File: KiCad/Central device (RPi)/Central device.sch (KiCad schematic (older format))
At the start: 1 part

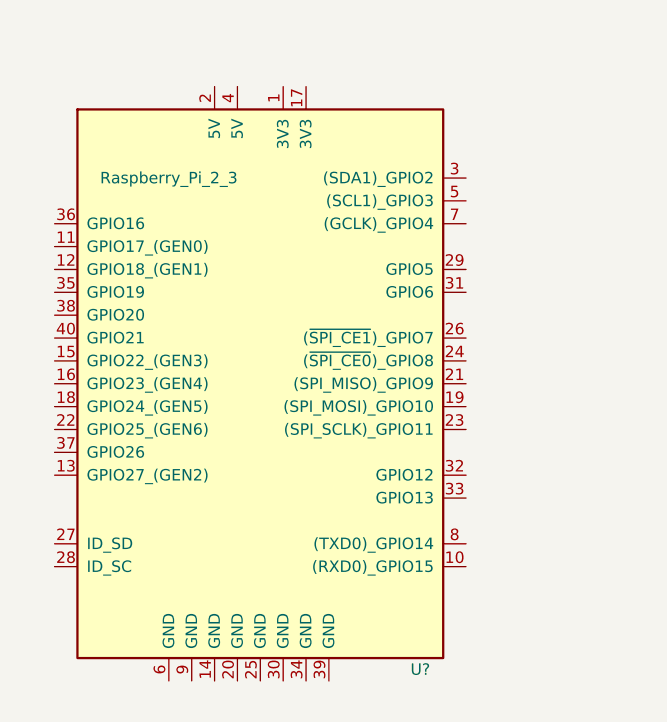
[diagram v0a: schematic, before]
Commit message: Added DHT11
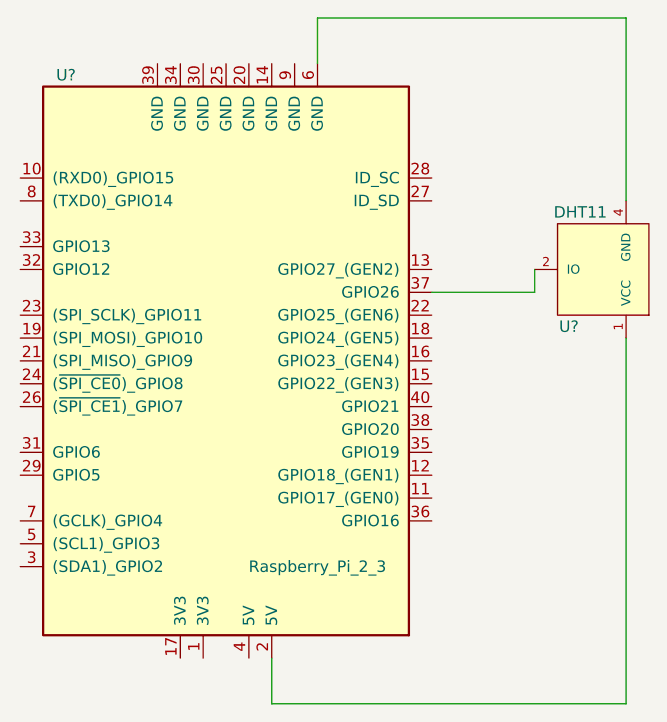
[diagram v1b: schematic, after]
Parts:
- added U?: DHT11, symbol DHT11
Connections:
- net at U?.2 (5V): now also U?.1 (VCC)
- net at U?.37 (GPIO26): now also U?.2 (IO)
- net at U?.6 (GND): now also U?.4 (GND)
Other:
- moved on the sheet: U?
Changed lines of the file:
@@
 LIBS:contrib
 LIBS:valves
+LIBS:sensors
+LIBS:Central device-cache
 EELAYER 25 0
 EELAYER END
@@
 L Raspberry_Pi_2_3 U?
 U 1 1 59353BE3
-P 3700 3100
-F 0 "U?" H 4400 1850 50  0000 C CNN
-F 1 "Raspberry_Pi_2_3" H 3300 4000 50  0000 C CNN
-F 2 "Pin_Headers:Pin_Header_Straight_2x20" H 4700 4350 50  0001 C CNN
-F 3 "" H 3750 2950 50  0001 C CNN
-	1    3700 3100
-	1    0    0    -1
+P 3550 3000
+F 0 "U?" H 4250 1750 50  0000 C CNN
+F 1 "Raspberry_Pi_2_3" H 3150 3900 50  0000 C CNN
+F 2 "Pin_Headers:Pin_Header_Straight_2x20" H 4550 4250 50  0001 C CNN
+F 3 "" H 3600 2850 50  0001 C CNN
+	1    3550 3000
+	-1   0    0    1
 $EndComp
+$Comp
+L DHT11 U?
+U 1 1 593E3675
+P 5200 2600
+F 0 "U?" H 5350 2850 50  0000 C CNN
+F 1 "DHT11" H 5300 2350 50  0000 C CNN
+F 2 "" H 5350 2850 50  0001 C CNN
+F 3 "" H 5350 2850 50  0001 C CNN
+	1    5200 2600
+	-1   0    0    1
+$EndComp
+Wire Wire Line
+	3750 4300 3750 4500
+Wire Wire Line
+	3750 4500 5300 4500
+Wire Wire Line
+	5300 4500 5300 2900
+Wire Wire Line
+	5300 2300 5300 1500
+Wire Wire Line
+	5300 1500 3950 1500
+Wire Wire Line
+	3950 1500 3950 1700
+Wire Wire Line
+	4900 2600 4900 2700
+Wire Wire Line
+	4900 2700 4450 2700
 $EndSCHEMATC

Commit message: Almost finished kicad schema of central device
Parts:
- added DS?: LCD-016N002L, WC1602A, symbol LCD-016N002L
- added U?: PCF8574A, symbol PCF8574A
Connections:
- net at U?.3 ((SDA1)_GPIO2): now also U?.15 (SDA)
- net at U?.37 (GPIO26): no longer U?.2 (IO)
- net at U?.4 (5V): now also DS?.15 (LED+), DS?.2 (VDD), U?.16 (VDD)
- net at U?.5 ((SCL1)_GPIO3): now also U?.14 (SCL)
- net at U?.7 ((GCLK)_GPIO4): now also U?.2 (IO)
- net at U?.9 (GND): now also DS?.1 (VSS), DS?.16 (LED-), U?.8 (VSS)
- new net: DS?.12 (D5), U?.10 (P5)
- new net: DS?.13 (D6), U?.11 (P6)
- new net: DS?.14 (D7), U?.12 (P7)
- new net: DS?.7 (D0), U?.4 (P0)
- new net: DS?.8 (D1), U?.5 (P1)
- new net: DS?.9 (D2), U?.6 (P2)
- new net: DS?.10 (D3), U?.7 (P3)
- new net: DS?.11 (D4), U?.9 (P4)
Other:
- note added: "These two components are already unified in one single product.\nConnection between them come from my imagination.\n(Need help to get the good connection)."
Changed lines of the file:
@@
 	3950 1500 3950 1700
 Wire Wire Line
-	4900 2600 4900 2700
+	4900 2600 4800 2600
 Wire Wire Line
-	4900 2700 4450 2700
+	4800 2600 4800 4450
+Wire Wire Line
+	4800 4450 2500 4450
+Wire Wire Line
+	2500 4450 2500 3700
+Wire Wire Line
+	2500 3700 2650 3700
+$Comp
+L PCF8574A U?
+U 1 1 5946C7CE
+P 6600 3800
+F 0 "U?" H 6250 4400 50  0000 L CNN
+F 1 "PCF8574A" H 6700 4400 50  0000 L CNN
+F 2 "" H 6600 3800 50  0000 C CNN
+F 3 "" H 6600 3800 50  0000 C CNN
+	1    6600 3800
+	1    0    0    -1
+$EndComp
+Wire Wire Line
+	6100 3400 4850 3400
+Wire Wire Line
+	4850 3400 4850 4400
+Wire Wire Line
+	4850 4400 2550 4400
+Wire Wire Line
+	2550 4400 2550 3800
+Wire Wire Line
+	2550 3800 2650 3800
+Wire Wire Line
+	6100 3500 4900 3500
+Wire Wire Line
+	4900 3500 4900 4350
+Wire Wire Line
+	4900 4350 2600 4350
+Wire Wire Line
+	2600 4350 2600 3900
+Wire Wire Line
+	2600 3900 2650 3900
+Wire Wire Line
+	3650 4300 3650 4550
+Wire Wire Line
+	6600 4550 6600 4500
+Wire Wire Line
+	6600 3100 6600 3050
+Wire Wire Line
+	5950 3050 9250 3050
+Wire Wire Line
+	5950 3050 5950 4550
+$Comp
+L LCD-016N002L DS?
+U 1 1 5946CA00
+P 8600 2350
+F 0 "DS?" H 7800 2750 50  0000 C CNN
+F 1 "LCD-016N002L" H 9300 2750 50  0000 C CNN
+F 2 "WC1602A" H 8600 2300 50  0000 C CIN
+F 3 "" H 8600 2350 50  0000 C CNN
+	1    8600 2350
+	1    0    0    -1
+$EndComp
+Wire Wire Line
+	7950 3050 7950 2850
+Connection ~ 6600 3050
+Wire Wire Line
+	7850 4550 7850 2850
+Wire Wire Line
+	7100 3400 8450 3400
+Wire Wire Line
+	8450 3400 8450 2850
+Wire Wire Line
+	7100 3500 8550 3500
+Wire Wire Line
+	8550 3500 8550 2850
+Wire Wire Line
+	7100 3600 8650 3600
+Wire Wire Line
+	8650 3600 8650 2850
+Wire Wire Line
+	7100 3700 8750 3700
+Wire Wire Line
+	8750 3700 8750 2850
+Wire Wire Line
+	7100 3800 8850 3800
+Wire Wire Line
+	8850 3800 8850 2850
+Wire Wire Line
+	7100 3900 8950 3900
+Wire Wire Line
+	8950 3900 8950 2850
+Wire Wire Line
+	7100 4000 9050 4000
+Wire Wire Line
+	9050 4000 9050 2850
+Wire Wire Line
+	7100 4100 9150 4100
+Wire Wire Line
+	9150 4100 9150 2850
+Wire Wire Line
+	5950 4550 3650 4550
+Wire Wire Line
+	6200 4550 9350 4550
+Wire Wire Line
+	3850 1700 3850 1450
+Wire Wire Line
+	3850 1450 5500 1450
+Wire Wire Line
+	5500 1450 5500 4500
+Wire Wire Line
+	6200 4500 6200 4550
+Connection ~ 6600 4550
+Wire Wire Line
+	5500 4500 6200 4500
+Wire Wire Line
+	9250 3050 9250 2850
+Connection ~ 7950 3050
+Wire Wire Line
+	9350 4550 9350 2850
+Connection ~ 7850 4550
+Wire Notes Line
+	6050 1800 6050 4800
+Wire Notes Line
+	6050 4800 9750 4800
+Wire Notes Line
+	9750 4800 9750 1800
+Wire Notes Line
+	9750 1800 6050 1800
+Text Notes 6100 1750 0    60   ~ 0
+These two components are already unified in one single product.\nConnection between them come from my imagination.\n(Need help to get the good connection).
 $EndSCHEMATC

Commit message: Added relay
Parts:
- added K?: FINDER-32.21-x000, Relays_THT:Relay_SPST_Finder_32.21-x300, symbol FINDER-32.21-x000
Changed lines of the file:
@@
 LIBS:valves
 LIBS:sensors
+LIBS:switches
+LIBS:relays
 LIBS:Central device-cache
 EELAYER 25 0
@@
 Text Notes 6100 1750 0    60   ~ 0
 These two components are already unified in one single product.\nConnection between them come from my imagination.\n(Need help to get the good connection).
+$Comp
+L FINDER-32.21-x000 K?
+U 1 1 594776D9
+P 3450 5750
+F 0 "K?" H 3900 5900 50  0000 L CNN
+F 1 "FINDER-32.21-x000" H 3900 5800 50  0000 L CNN
+F 2 "Relays_THT:Relay_SPST_Finder_32.21-x300" H 4720 5720 50  0001 C CNN
+F 3 "" H 3450 5750 50  0001 C CNN
+	1    3450 5750
+	1    0    0    -1
+$EndComp
 $EndSCHEMATC

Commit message: Finished circuit draft (Central device)
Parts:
- added NPN1: Q_NPN_BCE, symbol Q_NPN_BCE
- gave numbers to parts that had none: 4
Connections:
- net at RPI1B+.29 (GPIO5): now also NPN1.1 (B)
- net at RPI1B+.39 (GND): now also NPN1.2 (C)
- net at LCD.15 (LED+), LCD.2 (VDD), LCDDriver.16 (VDD)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: now also RL1.A1
- net ToHeater: now reaches RL1.11
- net ToHeater: now also RL1.14
- net at RL1.A2: now also NPN1.3 (E)
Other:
- note added: "Unified component. Reverse engineered."
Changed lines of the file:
@@
 $EndDescr
 $Comp
-L Raspberry_Pi_2_3 U?
+L Raspberry_Pi_2_3 RPI1B+
 U 1 1 59353BE3
 P 3550 3000
-F 0 "U?" H 4250 1750 50  0000 C CNN
+F 0 "RPI1B+" H 4250 1750 50  0000 C CNN
 F 1 "Raspberry_Pi_2_3" H 3150 3900 50  0000 C CNN
 F 2 "Pin_Headers:Pin_Header_Straight_2x20" H 4550 4250 50  0001 C CNN
@@
 	2500 3700 2650 3700
 $Comp
-L PCF8574A U?
+L PCF8574A LCDDriver
 U 1 1 5946C7CE
 P 6600 3800
-F 0 "U?" H 6250 4400 50  0000 L CNN
+F 0 "LCDDriver" H 6250 4400 50  0000 L CNN
 F 1 "PCF8574A" H 6700 4400 50  0000 L CNN
 F 2 "" H 6600 3800 50  0000 C CNN
@@
 	2600 3900 2650 3900
 Wire Wire Line
-	3650 4300 3650 4550
+	3650 4300 3650 4850
 Wire Wire Line
 	6600 4550 6600 4500
@@
 	5950 3050 5950 4550
 $Comp
-L LCD-016N002L DS?
+L LCD-016N002L LCD
 U 1 1 5946CA00
 P 8600 2350
-F 0 "DS?" H 7800 2750 50  0000 C CNN
+F 0 "LCD" H 7800 2750 50  0000 C CNN
 F 1 "LCD-016N002L" H 9300 2750 50  0000 C CNN
 F 2 "WC1602A" H 8600 2300 50  0000 C CIN
@@
 These two components are already unified in one single product.\nConnection between them come from my imagination.\n(Need help to get the good connection).
 $Comp
-L FINDER-32.21-x000 K?
+L FINDER-32.21-x000 RL1
 U 1 1 594776D9
 P 3450 5750
-F 0 "K?" H 3900 5900 50  0000 L CNN
+F 0 "RL1" H 3900 5900 50  0000 L CNN
 F 1 "FINDER-32.21-x000" H 3900 5800 50  0000 L CNN
 F 2 "Relays_THT:Relay_SPST_Finder_32.21-x300" H 4720 5720 50  0001 C CNN
@@
 	1    0    0    -1
 $EndComp
+$Comp
+L Q_NPN_BCE NPN1
+U 1 1 594A1450
+P 2350 5750
+F 0 "NPN1" H 2550 5800 50  0000 L CNN
+F 1 "Q_NPN_BCE" H 2550 5700 50  0000 L CNN
+F 2 "" H 2550 5850 50  0000 C CNN
+F 3 "" H 2350 5750 50  0000 C CNN
+	1    2350 5750
+	1    0    0    -1
+$EndComp
+Wire Wire Line
+	2450 5950 2450 6400
+Wire Wire Line
+	2450 6400 3250 6400
+Wire Wire Line
+	3250 6400 3250 6050
+Wire Wire Line
+	3250 5450 3250 4850
+Wire Wire Line
+	3250 4850 3650 4850
+Connection ~ 3650 4550
+Wire Wire Line
+	2450 5550 2450 1450
+Wire Wire Line
+	2450 1450 3250 1450
+Wire Wire Line
+	3250 1450 3250 1700
+Wire Wire Line
+	2150 5750 2150 3500
+Wire Wire Line
+	2150 3500 2650 3500
+Wire Wire Line
+	3750 5450 3750 5250
+Wire Wire Line
+	3750 5250 5300 5250
+Wire Wire Line
+	5300 5250 5300 5800
+Wire Wire Line
+	3650 6050 3650 6300
+Wire Wire Line
+	3650 6300 5300 6300
+Wire Wire Line
+	5300 6300 5300 6150
+Text GLabel 5300 5800 2    60   Input ~ 0
+ToHeater
+Text GLabel 5300 6150 2    60   Input ~ 0
+ToHeater
+Wire Notes Line
+	1900 5100 5900 5100
+Wire Notes Line
+	5900 5100 5900 6700
+Wire Notes Line
+	5900 6700 1900 6700
+Wire Notes Line
+	1900 6700 1900 5100
+Text Notes 3750 6850 2    60   ~ 0
+Unified component. Reverse engineered.
 $EndSCHEMATC

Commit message: Finished circuit draft (Central device)
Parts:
- gave numbers to parts that had none: 1
- renumbered LCD to LCD1, LCDDriver to LCDDriver1, RPI1B+ to RPI1B+1
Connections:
- no-connect marks 0 -> 40
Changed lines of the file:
@@
 $EndDescr
 $Comp
-L Raspberry_Pi_2_3 RPI1B+
+L Raspberry_Pi_2_3 RPI1B+1
 U 1 1 59353BE3
 P 3550 3000
-F 0 "RPI1B+" H 4250 1750 50  0000 C CNN
+F 0 "RPI1B+1" H 4250 1750 50  0000 C CNN
 F 1 "Raspberry_Pi_2_3" H 3150 3900 50  0000 C CNN
 F 2 "Pin_Headers:Pin_Header_Straight_2x20" H 4550 4250 50  0001 C CNN
@@
 $EndComp
 $Comp
-L DHT11 U?
+L DHT11 U1
 U 1 1 593E3675
 P 5200 2600
-F 0 "U?" H 5350 2850 50  0000 C CNN
+F 0 "U1" H 5350 2850 50  0000 C CNN
 F 1 "DHT11" H 5300 2350 50  0000 C CNN
 F 2 "" H 5350 2850 50  0001 C CNN
@@
 	2500 3700 2650 3700
 $Comp
-L PCF8574A LCDDriver
+L PCF8574A LCDDriver1
 U 1 1 5946C7CE
 P 6600 3800
-F 0 "LCDDriver" H 6250 4400 50  0000 L CNN
+F 0 "LCDDriver1" H 6250 4400 50  0000 L CNN
 F 1 "PCF8574A" H 6700 4400 50  0000 L CNN
 F 2 "" H 6600 3800 50  0000 C CNN
@@
 	5950 3050 5950 4550
 $Comp
-L LCD-016N002L LCD
+L LCD-016N002L LCD1
 U 1 1 5946CA00
 P 8600 2350
-F 0 "LCD" H 7800 2750 50  0000 C CNN
+F 0 "LCD1" H 7800 2750 50  0000 C CNN
 F 1 "LCD-016N002L" H 9300 2750 50  0000 C CNN
 F 2 "WC1602A" H 8600 2300 50  0000 C CIN
@@
 Text Notes 3750 6850 2    60   ~ 0
 Unified component. Reverse engineered.
+NoConn ~ 3550 5450
+NoConn ~ 3350 1700
+NoConn ~ 3450 1700
+NoConn ~ 3550 1700
+NoConn ~ 3650 1700
+NoConn ~ 3750 1700
+NoConn ~ 2650 2200
+NoConn ~ 2650 2300
+NoConn ~ 2650 2500
+NoConn ~ 2650 2600
+NoConn ~ 2650 2800
+NoConn ~ 2650 2900
+NoConn ~ 2650 3000
+NoConn ~ 2650 3100
+NoConn ~ 2650 3200
+NoConn ~ 2650 3400
+NoConn ~ 3350 4300
+NoConn ~ 3450 4300
+NoConn ~ 4450 3700
+NoConn ~ 4450 3600
+NoConn ~ 4450 3500
+NoConn ~ 4450 3400
+NoConn ~ 4450 3300
+NoConn ~ 4450 3200
+NoConn ~ 4450 3100
+NoConn ~ 4450 3000
+NoConn ~ 4450 2900
+NoConn ~ 4450 2800
+NoConn ~ 4450 2700
+NoConn ~ 4450 2600
+NoConn ~ 4450 2300
+NoConn ~ 4450 2200
+NoConn ~ 6100 3700
+NoConn ~ 6100 3800
+NoConn ~ 6100 3900
+NoConn ~ 6100 4200
+NoConn ~ 8050 2850
+NoConn ~ 8150 2850
+NoConn ~ 8250 2850
+NoConn ~ 8350 2850
 $EndSCHEMATC

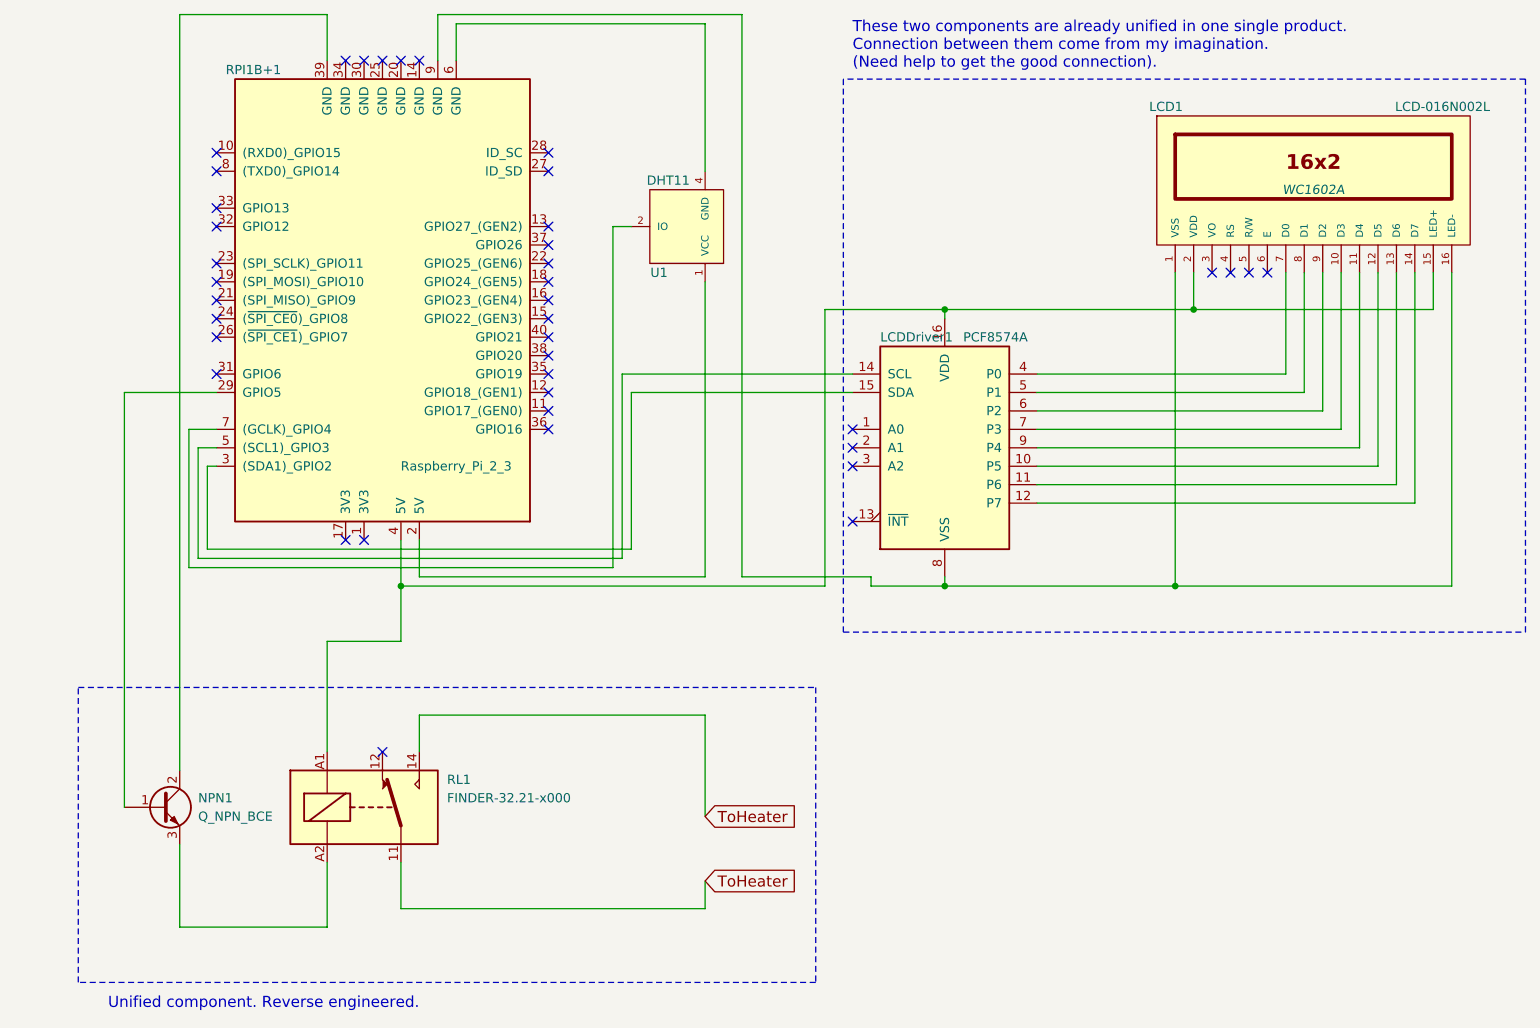
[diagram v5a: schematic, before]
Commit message: Added PDF of schema with corrections
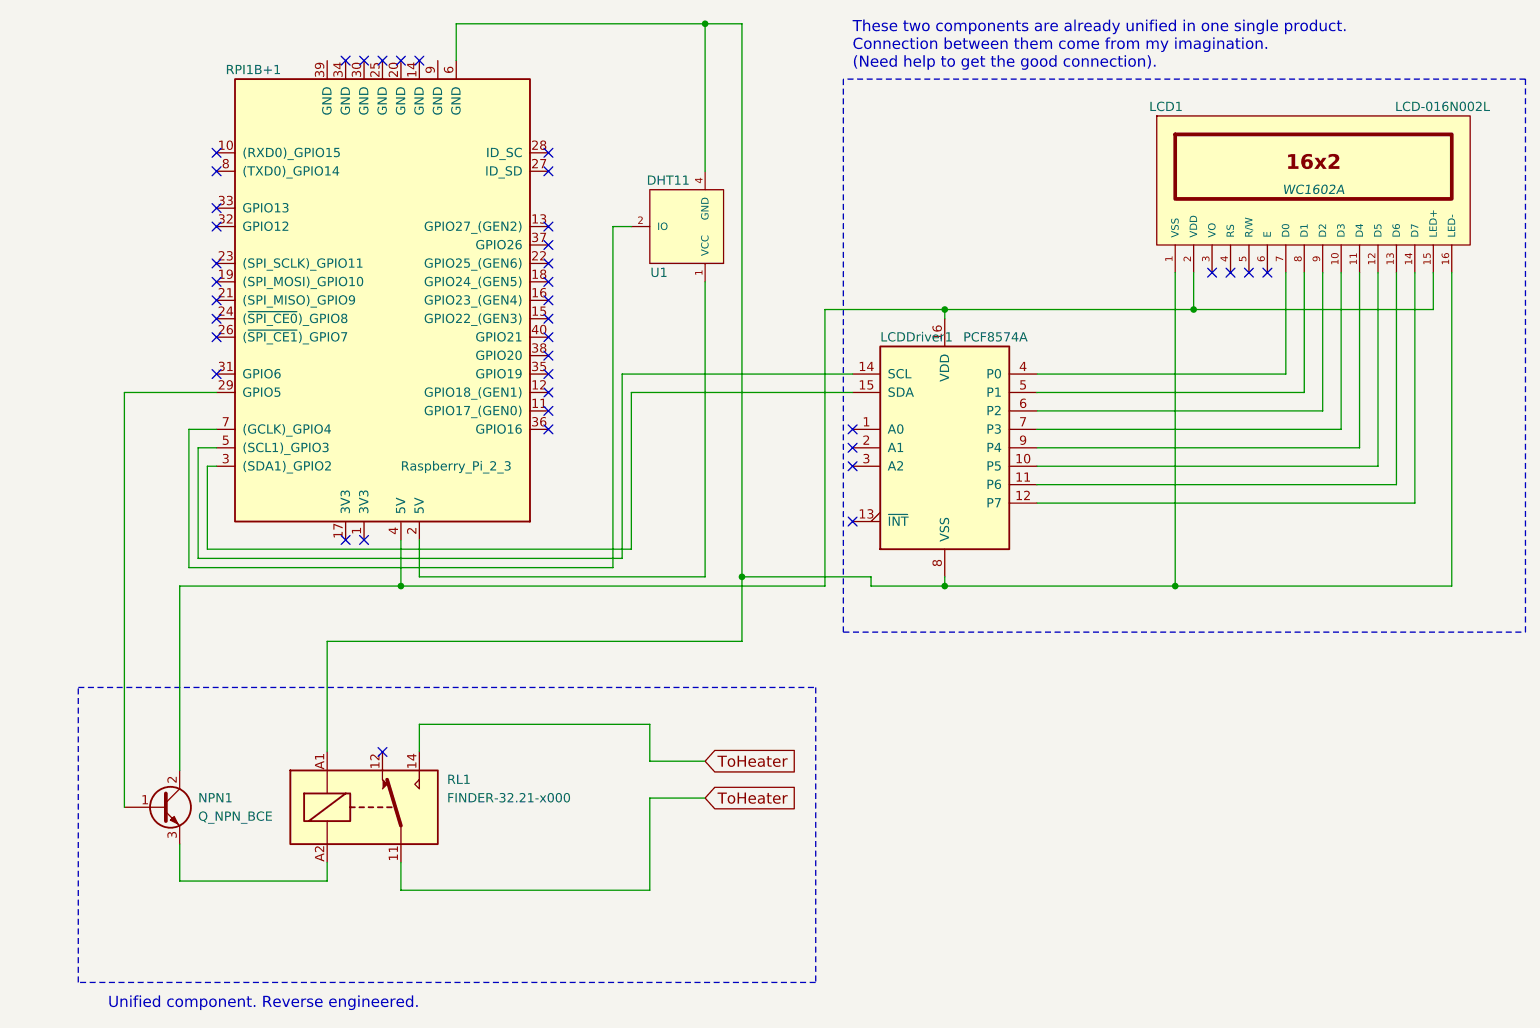
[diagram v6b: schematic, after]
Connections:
- net at RPI1B+1.39 (GND): no longer NPN1.2 (C)
- net at LCD1.15 (LED+), LCD1.2 (VDD), LCDDriver1.16 (VDD)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: now also NPN1.2 (C); no longer RL1.A1
- net at RPI1B+1.6 (GND), U1.4 (GND): now also LCD1.1 (VSS), LCD1.16 (LED-), LCDDriver1.8 (VSS), RL1.A1
- now unconnected: RPI1B+1.9 (GND)
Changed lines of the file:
@@
 	5300 2300 5300 1500
 Wire Wire Line
-	5300 1500 3950 1500
+	3950 1500 5300 1500
+Wire Wire Line
+	5300 1500 5500 1500
 Wire Wire Line
 	3950 1500 3950 1700
@@
 	2600 3900 2650 3900
 Wire Wire Line
-	3650 4300 3650 4850
-Wire Wire Line
 	6600 4550 6600 4500
 Wire Wire Line
 	6600 3100 6600 3050
 Wire Wire Line
-	5950 3050 9250 3050
-Wire Wire Line
-	5950 3050 5950 4550
+	5950 3050 6600 3050
+Wire Wire Line
+	6600 3050 7950 3050
+Wire Wire Line
+	7950 3050 9250 3050
+Wire Wire Line
+	5950 4550 5950 3050
 $Comp
 L LCD-016N002L LCD1
@@
 	9150 4100 9150 2850
 Wire Wire Line
-	5950 4550 3650 4550
-Wire Wire Line
-	6200 4550 9350 4550
-Wire Wire Line
-	3850 1700 3850 1450
-Wire Wire Line
-	3850 1450 5500 1450
-Wire Wire Line
-	5500 1450 5500 4500
+	6200 4550 6600 4550
+Wire Wire Line
+	6600 4550 7850 4550
+Wire Wire Line
+	7850 4550 9350 4550
 Wire Wire Line
 	6200 4500 6200 4550
@@
 $EndComp
 Wire Wire Line
-	2450 5950 2450 6400
-Wire Wire Line
-	2450 6400 3250 6400
-Wire Wire Line
-	3250 6400 3250 6050
+	2450 5950 2450 6150
+Wire Wire Line
+	2450 6150 3250 6150
+Wire Wire Line
+	3250 6150 3250 6050
 Wire Wire Line
 	3250 5450 3250 4850
 Wire Wire Line
-	3250 4850 3650 4850
-Connection ~ 3650 4550
-Wire Wire Line
-	2450 5550 2450 1450
-Wire Wire Line
-	2450 1450 3250 1450
-Wire Wire Line
-	3250 1450 3250 1700
-Wire Wire Line
 	2150 5750 2150 3500
 Wire Wire Line
 	2150 3500 2650 3500
-Wire Wire Line
-	3750 5450 3750 5250
-Wire Wire Line
-	3750 5250 5300 5250
-Wire Wire Line
-	5300 5250 5300 5800
-Wire Wire Line
-	3650 6050 3650 6300
-Wire Wire Line
-	3650 6300 5300 6300
-Wire Wire Line
-	5300 6300 5300 6150
-Text GLabel 5300 5800 2    60   Input ~ 0
+Text GLabel 5300 5500 2    60   Input ~ 0
 ToHeater
-Text GLabel 5300 6150 2    60   Input ~ 0
+Text GLabel 5300 5700 2    60   Input ~ 0
 ToHeater
 Wire Notes Line
@@
 NoConn ~ 8250 2850
 NoConn ~ 8350 2850
+Wire Wire Line
+	3650 4550 3650 4300
+Wire Wire Line
+	2450 4550 3650 4550
+Wire Wire Line
+	3650 4550 5950 4550
+Wire Wire Line
+	5500 1500 5500 4500
+Wire Wire Line
+	5500 4500 5500 4850
+Connection ~ 5300 1500
+Wire Wire Line
+	5500 4850 3250 4850
+Connection ~ 5500 4500
+Wire Wire Line
+	2450 5550 2450 4550
+Connection ~ 3650 4550
+Wire Wire Line
+	3650 6050 3650 6200
+Wire Wire Line
+	3650 6200 5000 6200
+Wire Wire Line
+	5000 6200 5000 5700
+Wire Wire Line
+	5000 5700 5300 5700
+Wire Wire Line
+	5300 5500 5000 5500
+Wire Wire Line
+	5000 5500 5000 5300
+Wire Wire Line
+	5000 5300 3750 5300
+Wire Wire Line
+	3750 5300 3750 5450
 $EndSCHEMATC
